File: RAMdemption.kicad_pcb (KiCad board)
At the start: 4 copper layers, 99 x 53.5 mm, 41 parts, among them J1 Conn_RAM_Expansion, U1 TC518512FTL-70, U10 TC518512FTL-70, U11 TC518512FTL-70, U12 TC518512FTL-70, U13 TC518512FTL-70, U14 TC518512FTL-70, U15 TC518512FTL-70, U16 TC518512FTL-70, U17 TC518512FTL-70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

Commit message: shuffle around files
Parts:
- C1, C10, C11, C12, C13, C14, C15, C16, C17, C18, C19, C2, C20, C3, C4, C5, C6, C7, C8, C9: footprint Capacitor_SMD:C_1206_3216Metric -> Capacitor_SMD:C_1206_3216Metric_Pad1.33x1.80mm_HandSolder
- J1: footprint RAMdemption:TE_5-104652-7 -> RAMdemption:TE_5-104652-7_NoHoles
- moved C8 58.0 mm to (154.2, 103.5), turned to 0 degrees
- moved C6 55.9 mm to (208.8, 123.3), turned to -90 degrees
- moved U20 31.7 mm to (154.7, 87.0), turned to -90 degrees
- moved U12 29.1 mm to (154.5, 115.3), turned to 0 degrees
- moved C9 22.4 mm to (136.2, 103.5)
- moved C17 17.4 mm to (136.2, 103.5), turned to 0 degrees
- moved U16 14.2 mm to (140.3, 115.3)
- moved C14 13.5 mm to (154.2, 103.5), turned to 0 degrees
- moved C7 8.70 mm to (163.9, 114.7), turned to -90 degrees
- moved C2 8.38 mm to (208.8, 93.0)
- moved C11 8.38 mm to (208.8, 114.9), turned to 90 degrees
- moved C1 7.37 mm to (142.9, 103.5), turned to 0 degrees
- moved C18 6.86 mm to (142.9, 103.5)
- moved C19 2.80 mm to (208.8, 84.7)
- moved U17 1.05 mm to (122.2, 110.4)
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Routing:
- net +5V: track 128.8 -> 432.9 mm, vias 20 -> 28
- net /RAM Bank 1/A18: track 127.3 -> 181.0 mm, vias 12 -> 15
- net /RAM Bank 1/A16: track 129.4 -> 176.9 mm
- net /RAM Bank 1/A3: track 121.1 -> 167.8 mm
- net /RAM Bank 1/A2: track 121.3 -> 166.9 mm
- net /RAM Bank 1/A0: track 120.4 -> 165.9 mm
- net /RAM Bank 1/A14: track 130.4 -> 173.3 mm
- net /RAM Bank 1/A17: track 122.8 -> 163.8 mm
- net /RAM Bank 1/A15: track 124.6 -> 165.5 mm, vias 13 -> 12
- net /RAM Bank 1/A12: track 131.7 -> 172.0 mm
- net /RAM Bank 1/A1: track 127.8 -> 165.8 mm
- net /RAM Bank 1/A7: track 134.0 -> 171.2 mm
- net /RAM Bank 1/A6: track 136.0 -> 170.3 mm
- net /RAM Bank 1/A9: track 125.8 -> 159.0 mm, vias 13 -> 12
- net /RAM Bank 1/A5: track 137.2 -> 169.5 mm
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- removed copper zone on In2.Cu, net +5V
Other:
- outline, holes or cut-outs redrawn

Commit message: lots of address routing (with some tricks)
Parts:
- U10, U14, U18, U2, U20, U4, U6: footprint Package_SO:TSOP-II-32_21.0x10.2mm_P1.27mm -> RAMdemption:TSOP-II-32_Repinned
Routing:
- net /RAM Bank 1/A18: track 181.0 -> 266.1 mm
- net /RAM Bank 1/A16: track 176.9 -> 257.9 mm
- net /RAM Bank 1/A15: track 165.5 -> 244.9 mm
- net /RAM Bank 1/A14: track 173.3 -> 252.4 mm
- net /RAM Bank 1/A12: track 172.0 -> 248.4 mm
- net /RAM Bank 1/A17: track 163.8 -> 239.1 mm
- net /RAM Bank 1/A7: track 171.2 -> 244.9 mm
- net /RAM Bank 1/A13: track 160.5 -> 231.8 mm
- net /RAM Bank 1/A6: track 170.3 -> 241.2 mm
- net /RAM Bank 1/A8: track 159.4 -> 227.6 mm
- net /RAM Bank 1/A5: track 169.5 -> 237.5 mm
- net /RAM Bank 1/A9: track 159.0 -> 224.5 mm
- net /RAM Bank 1/A4: track 168.8 -> 234.2 mm
- net /RAM Bank 1/A3: track 167.8 -> 230.4 mm
- net /RAM Bank 1/A11: track 157.3 -> 218.8 mm
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
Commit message: addresses done?!
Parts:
- moved C7 1.52 mm to (163.9, 113.2)
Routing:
- net /RAM Bank 1/A10: track 212.4 -> 240.4 mm
- net /RAM Bank 1/A0: track 219.5 -> 247.2 mm
- net /RAM Bank 1/A11: track 218.8 -> 243.2 mm
- net /RAM Bank 1/A1: track 224.0 -> 248.4 mm
- net /RAM Bank 1/A9: track 224.5 -> 247.4 mm
- net /RAM Bank 1/A2: track 226.6 -> 249.4 mm
- net /RAM Bank 1/A8: track 227.6 -> 249.5 mm
- net /RAM Bank 1/A13: track 231.8 -> 252.3 mm
- net /RAM Bank 1/A3: track 230.4 -> 250.7 mm
- net /RAM Bank 1/A17: track 239.1 -> 257.9 mm
- net /RAM Bank 1/A4: track 234.2 -> 252.7 mm
- net /RAM Bank 1/A15: track 244.9 -> 262.5 mm
- net /RAM Bank 1/A5: track 237.5 -> 254.3 mm
- net /RAM Bank 1/A6: track 241.2 -> 256.1 mm
- net /RAM Bank 1/A7: track 244.9 -> 258.0 mm
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
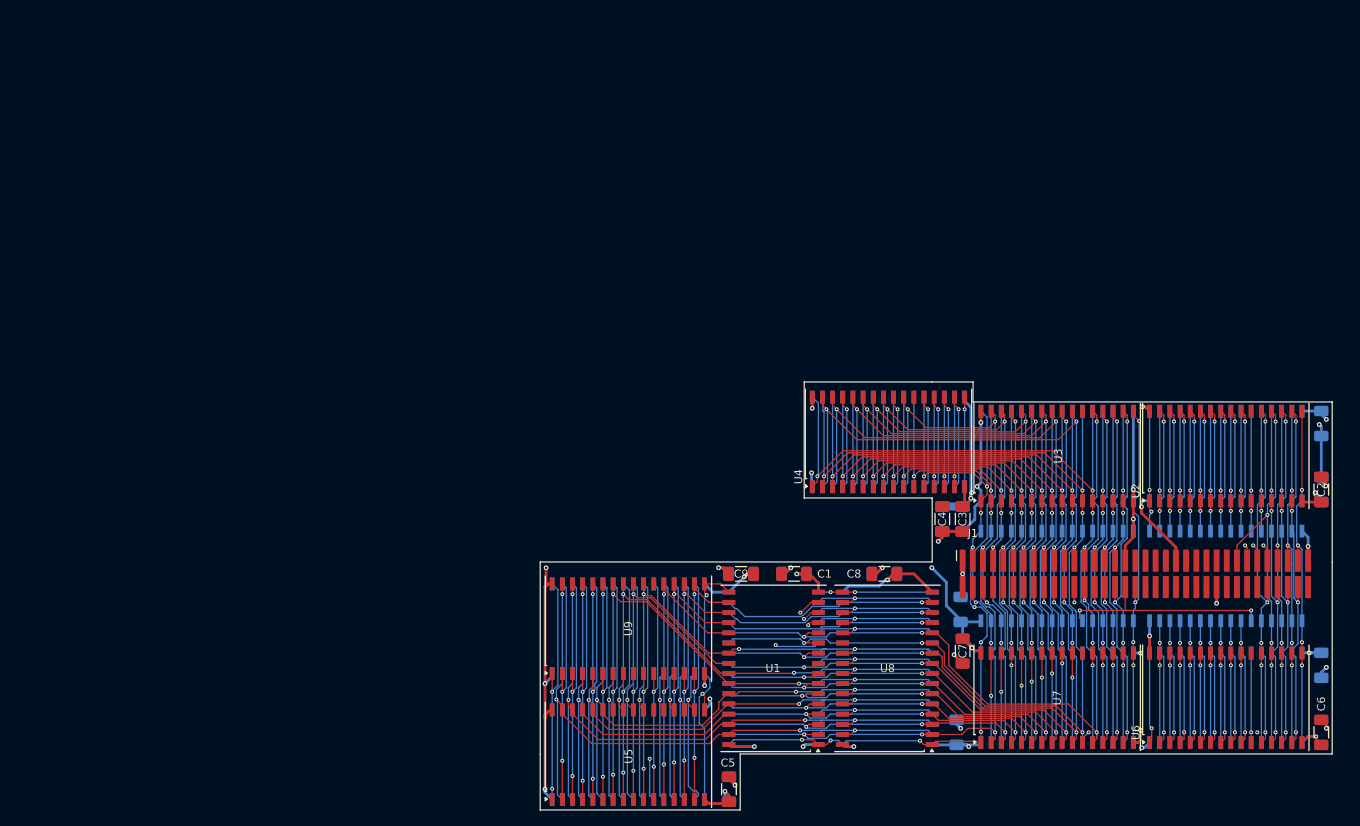
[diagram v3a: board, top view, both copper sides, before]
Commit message: just fifteen left unrouted
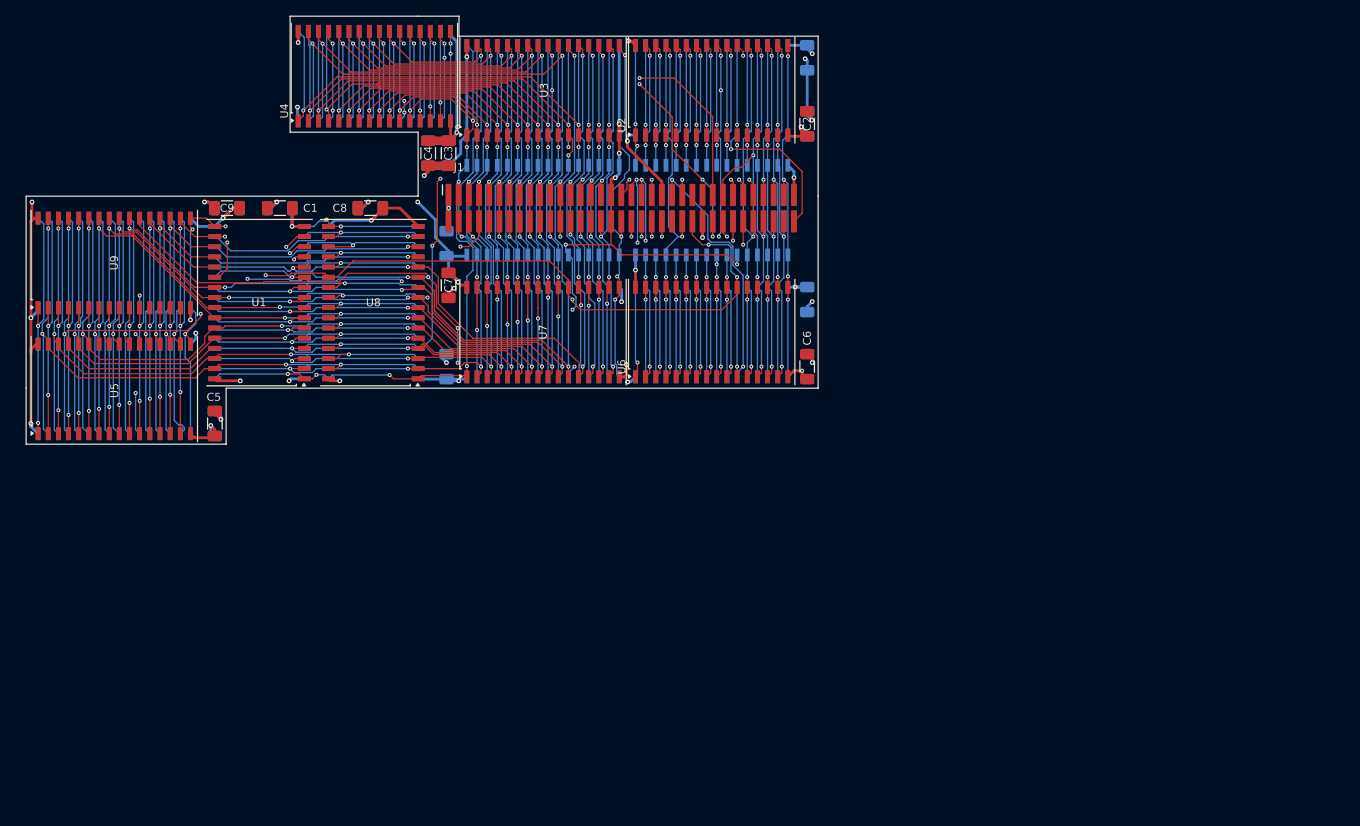
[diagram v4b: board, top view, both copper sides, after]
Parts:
- moved U1 78.9 mm to (76.0, 69.6)
- moved U16 78.9 mm to (76.0, 69.6)
- moved C1 78.9 mm to (78.6, 57.8)
- moved C10 78.9 mm to (97.1, 50.9)
- moved C11 78.9 mm to (144.5, 69.2)
- moved C14 78.9 mm to (89.9, 57.8)
- moved C15 78.9 mm to (144.5, 47.2)
- moved C18 78.9 mm to (78.6, 57.8)
- moved C2 78.9 mm to (144.5, 47.2)
- moved C20 78.9 mm to (99.7, 50.9)
- moved C3 78.9 mm to (99.7, 50.9)
- moved C4 78.9 mm to (97.1, 50.9)
- moved C6 78.9 mm to (144.5, 77.6)
- moved C7 78.9 mm to (99.7, 67.4)
- moved C8 78.9 mm to (89.9, 57.8)
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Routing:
- net ~{CS6}: track 0.00 -> 129.6 mm, vias 0 -> 5
- net ~{CS2}: track 1.91 -> 121.3 mm, vias 1 -> 5
- net ~{CS4}: track 23.0 -> 124.6 mm, vias 2 -> 6
- net ~{CS3}: track 0.00 -> 98.9 mm, vias 0 -> 5
- net ~{OE}: track 144.6 -> 235.7 mm, vias 11 -> 17
- net /~{WE3}: track 28.0 -> 106.5 mm, vias 2 -> 6
- net /~{WE0}: track 49.7 -> 109.5 mm, vias 2 -> 4
- net /RAM Bank 1/D2: track 56.2 -> 113.6 mm, vias 3 -> 5
- net /RAM Bank 1/D0: track 57.1 -> 114.0 mm, vias 3 -> 5
- net /RAM Bank 1/D3: track 34.0 -> 89.2 mm, vias 2 -> 4
- net /RAM Bank 1/D28: track 28.0 -> 78.5 mm, vias 2 -> 6
- net /RAM Bank 1/D1: track 56.7 -> 106.1 mm, vias 3 -> 4
- net /RAM Bank 1/D27: track 25.4 -> 72.3 mm, vias 3 -> 5
- net ~{CS5}: track 59.7 -> 105.0 mm, vias 4 -> 6
- net /RAM Bank 1/D26: track 40.2 -> 84.6 mm
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
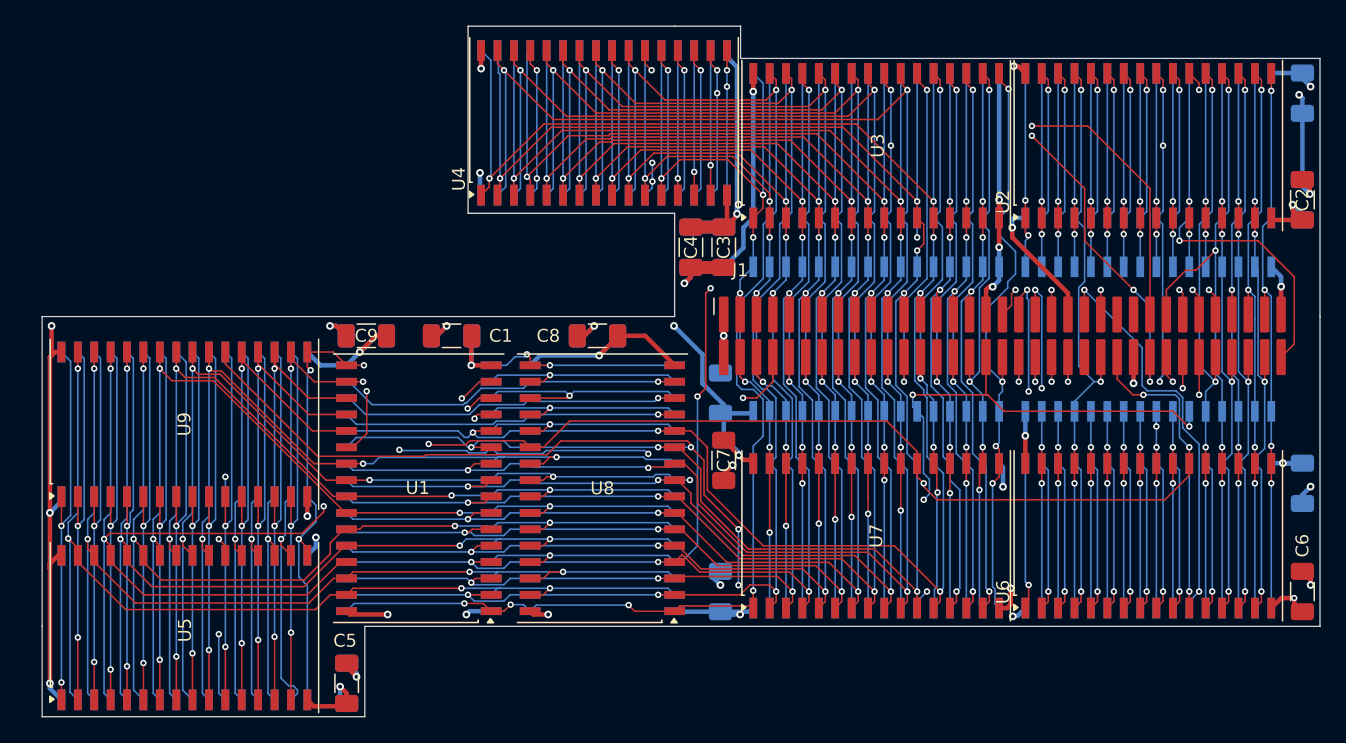
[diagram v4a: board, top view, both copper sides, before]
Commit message: routed all except UUW data lines
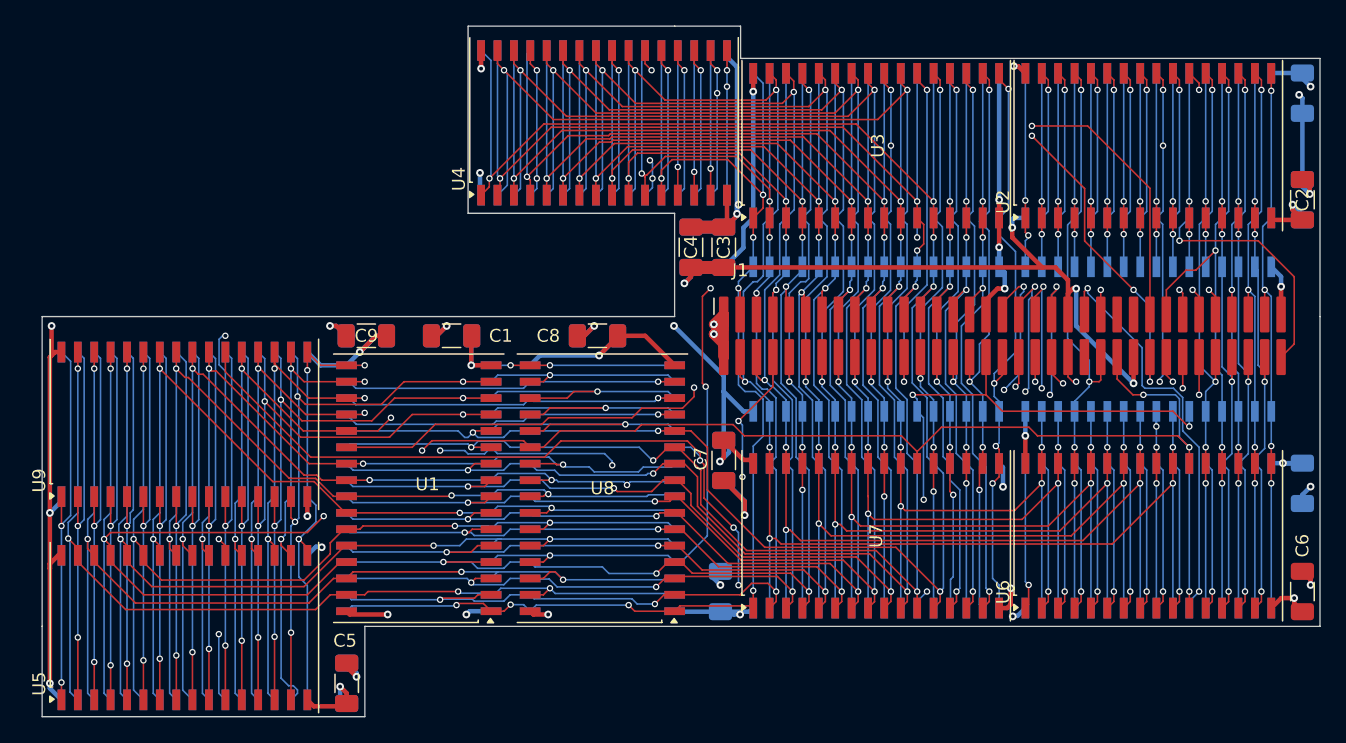
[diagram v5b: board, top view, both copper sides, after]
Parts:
- U1, U13, U17, U5, U9: footprint Package_SO:TSOP-II-32_21.0x10.2mm_P1.27mm -> RAMdemption:TSOP-II-32_Data0
- moved C16 5.21 mm to (99.7, 67.4), turned to -90 degrees
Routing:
- net /RAM Bank 1/D5: track 38.3 -> 103.6 mm, vias 3 -> 5
- net /RAM Bank 1/D7: track 41.8 -> 106.6 mm, vias 3 -> 5
- net /RAM Bank 1/D6: track 40.1 -> 102.3 mm, vias 3 -> 4
- net /RAM Bank 1/D4: track 38.9 -> 99.1 mm, vias 4 -> 5
- net +5V: track 482.8 -> 519.9 mm, vias 26 -> 27
- net /RAM Bank 1/D2: track 113.6 -> 101.9 mm
- net /RAM Bank 1/D1: track 106.1 -> 96.5 mm
- net /RAM Bank 1/D0: track 114.0 -> 106.7 mm, vias 5 -> 6
- net /RAM Bank 1/D31: track 30.9 -> 36.8 mm
- net /~{WE0}: track 109.5 -> 115.1 mm, vias 4 -> 5
- net GND: track 122.4 -> 127.8 mm, vias 21 -> 22
- net /RAM Bank 1/D3: track 89.2 -> 93.9 mm, vias 4 -> 5
- net /RAM Bank 1/D30: track 30.4 -> 34.7 mm
- net ~{OE}: track 235.7 -> 238.7 mm
- net ~{CS3}: track 98.9 -> 96.5 mm, vias 5 -> 4
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
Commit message: routing complete
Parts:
- U10, U14, U18, U2, U6: footprint RAMdemption:TSOP-II-32_Repinned -> RAMdemption:TSOP-II-32_ReversedAddr
- U12, U16, U8: footprint Package_SO:TSOP-II-32_21.0x10.2mm_P1.27mm -> RAMdemption:TSOP-II-NormalAddr-Data3
- U20, U4: footprint RAMdemption:TSOP-II-32_Repinned -> RAMdemption:TSOP-II-32_ReversedAddr_Data3
- moved U12 0.38 mm to (89.9, 69.6)
- moved U8 0.38 mm to (89.9, 69.6)
- moved C7 0.13 mm to (99.8, 67.4)
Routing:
- net /RAM Bank 1/D31: track 36.8 -> 150.7 mm
- net /RAM Bank 1/D29: track 33.8 -> 147.5 mm
- net /RAM Bank 1/D30: track 34.7 -> 147.3 mm
- net /RAM Bank 1/D28: track 78.5 -> 144.9 mm, vias 6 -> 3
- net /RAM Bank 1/D26: track 83.3 -> 136.9 mm
- net /RAM Bank 1/D25: track 82.7 -> 134.5 mm
- net /RAM Bank 1/D24: track 82.7 -> 133.5 mm, vias 3 -> 4
- net /RAM Bank 1/D27: track 71.2 -> 117.2 mm
- net ~{CS6}: track 131.8 -> 124.8 mm
- net /RAM Bank 1/A18: track 267.5 -> 273.5 mm, vias 13 -> 14
- net GND: track 127.8 -> 123.0 mm
- net /RAM Bank 1/A0: track 250.0 -> 245.2 mm
- net +5V: track 519.9 -> 515.2 mm, vias 27 -> 28
- net /RAM Bank 1/A16: track 268.5 -> 264.3 mm
- net /RAM Bank 1/A2: track 252.9 -> 248.8 mm
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
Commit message: various improvements
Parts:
- moved C7 0.10 mm to (99.7, 67.4)
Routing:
- net +5V: track 515.2 -> 524.8 mm
- net /RAM Bank 1/A16: track 264.3 -> 271.6 mm
- net /RAM Bank 1/A12: track 260.7 -> 267.9 mm
- net /RAM Bank 1/A4: track 253.9 -> 260.5 mm
- net /RAM Bank 1/A6: track 257.9 -> 264.4 mm
- net /RAM Bank 1/A15: track 261.1 -> 266.8 mm
- net /RAM Bank 1/A2: track 248.8 -> 254.3 mm
- net ~{CS2}: track 119.0 -> 123.4 mm
- net /RAM Bank 1/A9: track 249.8 -> 254.1 mm
- net /RAM Bank 1/D24: track 133.5 -> 137.3 mm
- net /~{WE0}: track 112.6 -> 116.0 mm
- net /RAM Bank 1/A17: track 257.9 -> 261.1 mm
- net /RAM Bank 1/A13: track 253.4 -> 256.5 mm
- net ~{CS6}: track 124.8 -> 127.7 mm
- net ~{OE}: track 238.1 -> 240.7 mm
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
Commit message: fix drc
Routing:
- net +5V: track 524.8 -> 539.2 mm
- net /RAM Bank 1/A1: track 255.2 -> 250.0 mm
- net /RAM Bank 1/A4: track 260.5 -> 256.3 mm
- net /RAM Bank 1/A5: track 256.7 -> 252.6 mm
- net /RAM Bank 1/A7: track 260.3 -> 256.2 mm
- net /RAM Bank 1/A0: track 246.2 -> 242.3 mm
- net /RAM Bank 1/A6: track 264.4 -> 260.6 mm
- net /RAM Bank 1/A3: track 254.7 -> 250.9 mm
- net /RAM Bank 1/D6: track 102.8 -> 99.4 mm
- net /RAM Bank 1/A2: track 254.3 -> 250.9 mm
- net /RAM Bank 1/A12: track 267.9 -> 264.9 mm
- net /RAM Bank 1/D28: track 144.6 -> 147.6 mm
- net /RAM Bank 1/A13: track 256.5 -> 254.1 mm
- net /RAM Bank 1/D30: track 147.3 -> 149.3 mm
- net /~{WE3}: track 106.8 -> 104.8 mm
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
